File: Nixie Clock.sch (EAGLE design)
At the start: 149 parts, among them IC1_SECONDS_UNITS 4017N, IC2_SECONDS_TENS 4017N, IC3_MINUTES_UNITS 4017N, IC4_MINUTES_TENS 4017N, IC5_HOURS_UNITS 4017N, IC6_HOURS_TENS 4017N, IC7_AND 4081N, T0 MPSA42, T1 MPSA42, T10 MPSA42, T11 MPSA42, T12 MPSA42, T13 MPSA42, T14 MPSA42, T15 MPSA42, T16 MPSA42, T17 MPSA42, T18 MPSA42, T19 MPSA42, T2 MPSA42, T20 MPSA42, T21 MPSA42, T22 MPSA42, T23 MPSA42, T24 MPSA42, T25 MPSA42, T26 MPSA42, T27 MPSA42, T28 MPSA42, T29 MPSA42, T3 MPSA42, T30 MPSA42, T31 MPSA42, T32 MPSA42, T33 MPSA42, T34 MPSA42, T35 MPSA42, T36 MPSA42, T37 MPSA42, T38 MPSA42, T39 MPSA42, T4 MPSA42, T40 MPSA42, T41 MPSA42, T42 MPSA42, T43 MPSA42, T44 MPSA42, T5 MPSA42, T6 MPSA42, T7 MPSA42, T8 MPSA42, T9 MPSA42

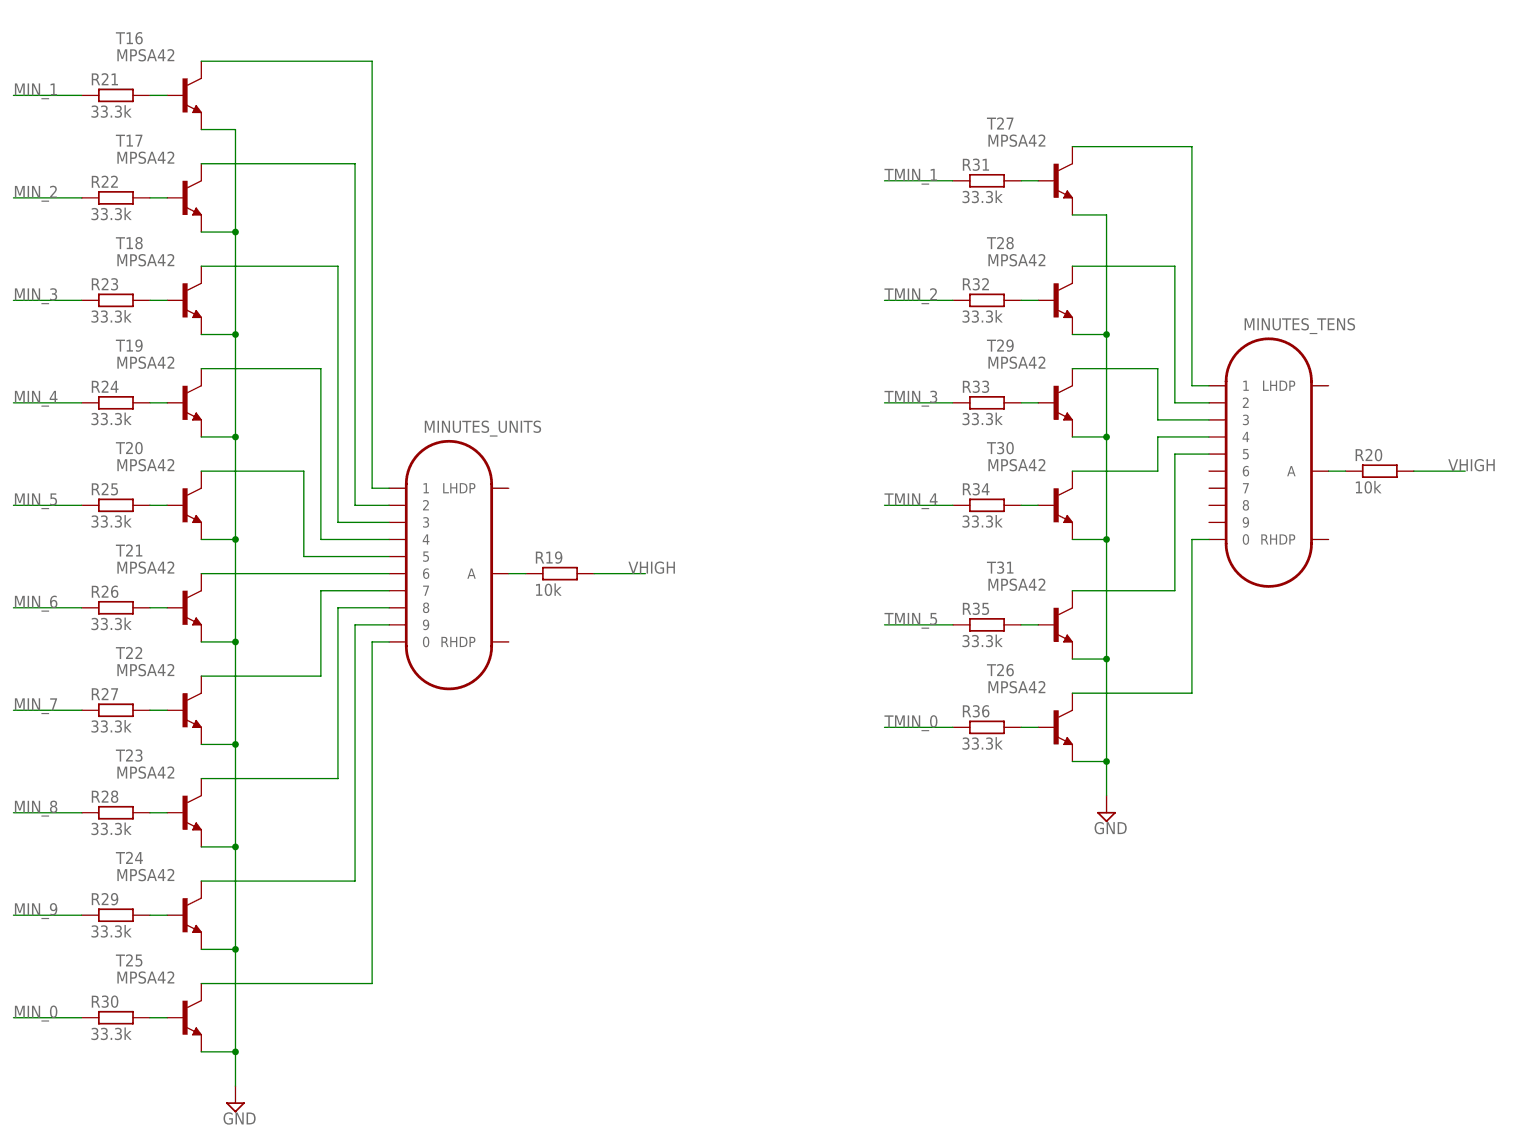
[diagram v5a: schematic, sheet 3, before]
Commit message: Add neon lamps
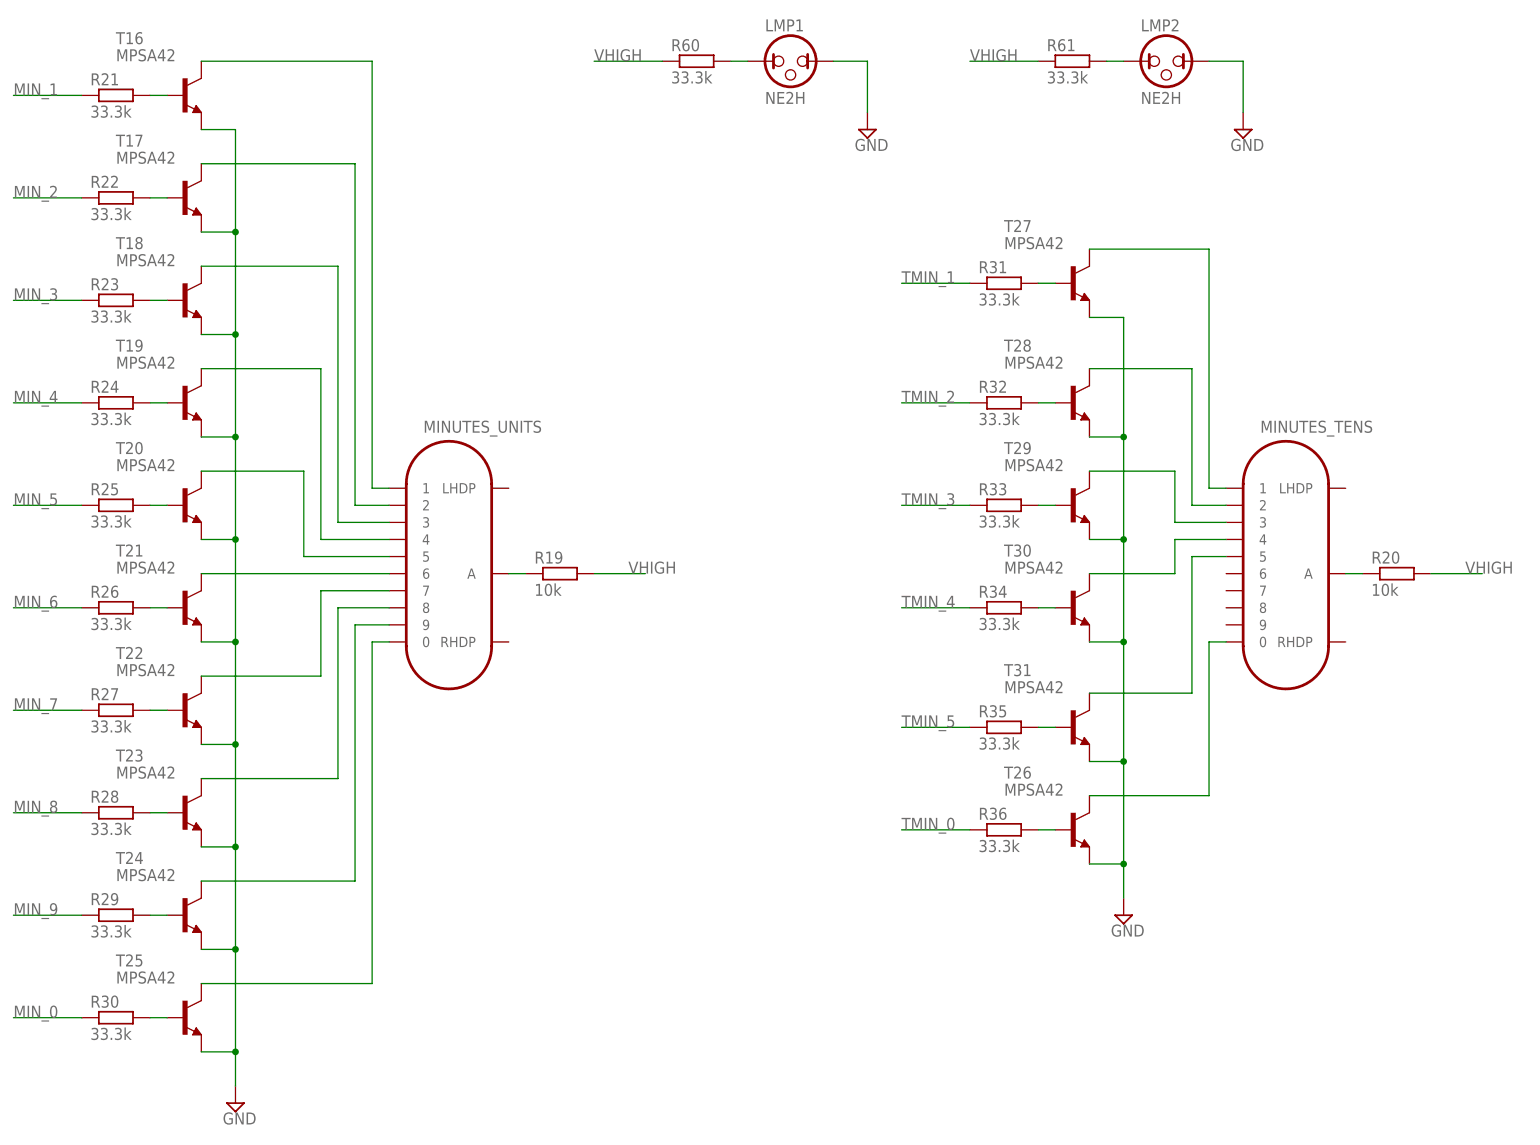
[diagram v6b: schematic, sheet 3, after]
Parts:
- added LMP1, LMP2: NE2H, PGT:NEON_LAMP
- added R60, R61: 33.3k, resistor:R-EU_0207/10
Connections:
- new net N$107: LMP2.1, R61.2
- new net N$108: LMP1.1, R60.2
- net GND: now also LMP1.2, LMP2.2
- net VHIGH: now also R60.1, R61.1
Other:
- moved on the sheet: MINUTES_TENS, R20, R31, R32, R33, R34, R35, R36, T26, T27, T28, T29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

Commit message: All Routed \o/
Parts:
- R1, R19, R2, R20, R37, R38, R60, R61: device resistor:R-EU_0207/10 -> resistor:R-EU_0207/2V
